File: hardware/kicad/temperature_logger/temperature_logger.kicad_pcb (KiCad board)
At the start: 2 copper layers, 40 x 64 mm, 45 parts, among them J1 SWD, J2 Power, J3 USB_B_Micro, J4 UART, Q1 Q_PMOS_DGS, SW1 UserBtn, U1 TMP112, U2 MX25R1635FM1IL0, U3 STM32L053C8Tx, U4 AMS1117-3.3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

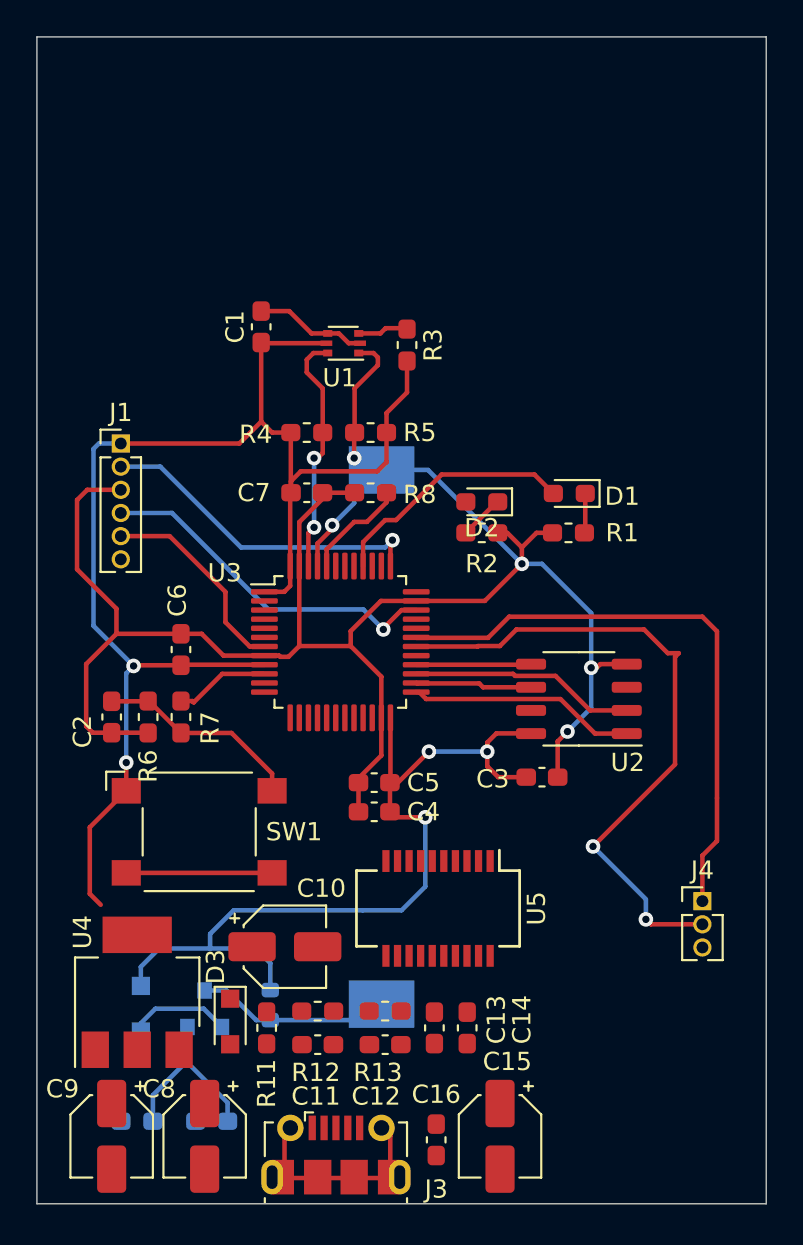
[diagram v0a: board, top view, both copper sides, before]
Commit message: Main rounting done for pass 2
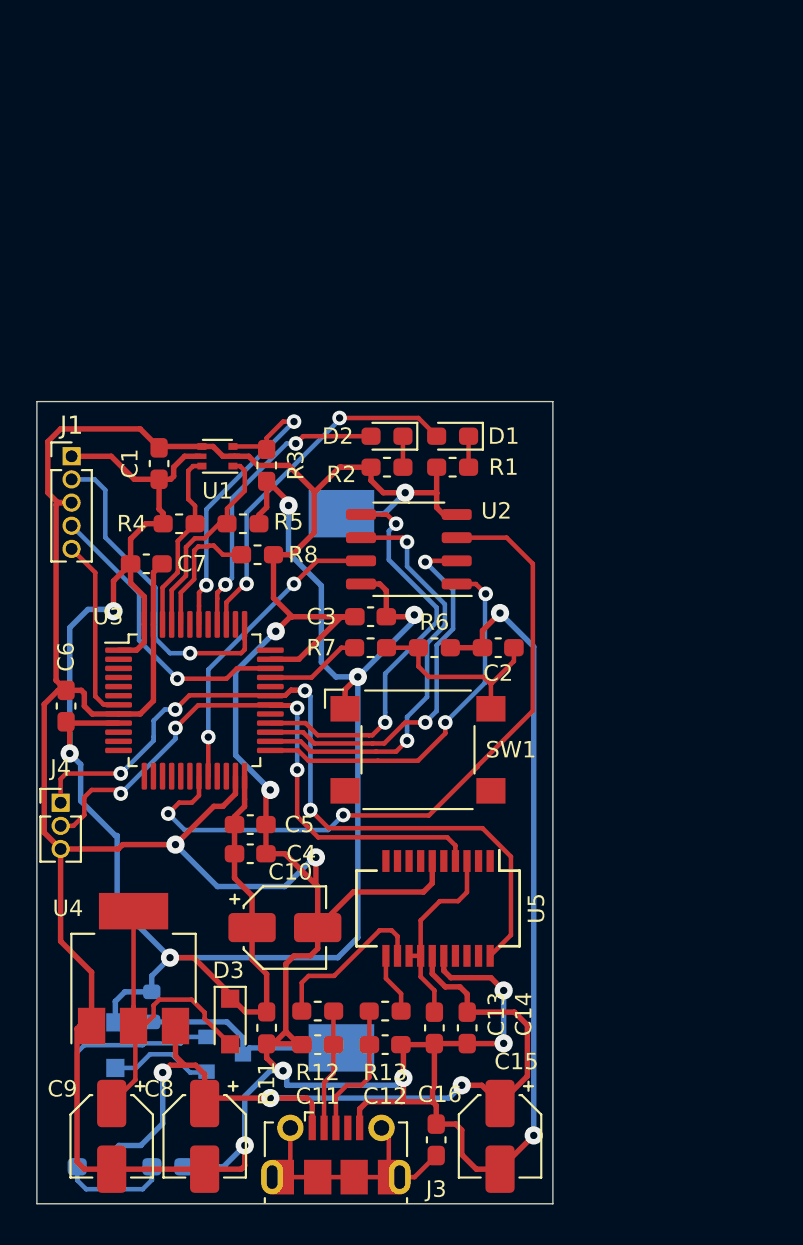
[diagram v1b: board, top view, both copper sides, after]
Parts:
- J1: footprint Connector_PinHeader_1.27mm:PinHeader_1x06_P1.27mm_Vertical -> Connector_PinHeader_1.27mm:PinHeader_1x05_P1.27mm_Vertical
- moved J4 35.6 mm to (131.3, 88.0)
- moved C2 21.5 mm to (155.3, 79.5), turned to 0 degrees
- moved R6 16.2 mm to (151.8, 79.5), turned to 0 degrees
- moved C3 12.9 mm to (148.3, 77.8), turned to 180 degrees
- moved SW1 12.8 mm to (150.9, 85.1)
- moved U2 12.4 mm to (150.4, 74.1)
- moved R7 11.1 mm to (148.3, 79.5), turned to 0 degrees
- moved R3 10.1 mm to (142.6, 69.5)
- moved C7 9.63 mm to (136.0, 74.9)
- moved C1 9.36 mm to (136.7, 69.4)
- moved U1 9.28 mm to (139.9, 69.0)
- moved U3 8.62 mm to (138.6, 82.4)
- moved R4 8.60 mm to (137.8, 72.7)
- moved R5 8.60 mm to (141.3, 72.7)
- moved R1 7.30 mm to (152.8, 69.6)
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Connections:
- U3 pad 10: /USER_BTN -> (no net)
- U3 pad 15: /USER_LED1 -> (no net)
- U3 pad 18: /TMP_ALERT -> (no net)
- U3 pad 33: (no net) -> /USER_BTN
- U3 pad 39: (no net) -> /USER_LED2
- U3 pad 40: /USER_LED2 -> /USER_LED1
- U3 pad 42: (no net) -> /TMP_ALERT
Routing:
- net GND: track 104.1 -> 268.6 mm, vias 3 -> 12
- net VBUS: track 0.00 -> 47.5 mm, vias 0 -> 3
- net /FLASH_WPN: track 0.00 -> 39.1 mm, vias 0 -> 2
- net Net-(C9-Pad1): track 0.00 -> 18.9 mm
- net /FLASH_SCLK: track 6.40 -> 23.3 mm, vias 0 -> 2
- net /FLASH_RSTN: track 0.00 -> 16.7 mm, vias 0 -> 2
- net /USER_LED1: track 0.00 -> 16.3 mm, vias 0 -> 2
- net /FLASH_SI: track 6.31 -> 22.3 mm, vias 0 -> 2
- net /TMP_ALERT: track 2.79 -> 17.7 mm, vias 0 -> 2
- net /USART1_RX: track 32.5 -> 44.1 mm, vias 0 -> 4
- net Net-(C13-Pad1): track 0.00 -> 10.9 mm
- net Net-(Q1-Pad2): track 10.2 -> 19.7 mm
- net Net-(R12-Pad2): track 0.00 -> 9.21 mm
- net /FLASH_SO: track 12.4 -> 21.0 mm, vias 0 -> 2
- net /FLASH_CSN: track 12.5 -> 20.8 mm, vias 0 -> 2
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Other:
- board size 40 x 64 mm -> 28.3 x 44 mm
- net class Power added: clearance 0.2, trace_width 0.3, via_dia 1, via_drill 0.4
- board text added: "TempPal v1.0"

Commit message: Hardware routing completed (verification required)
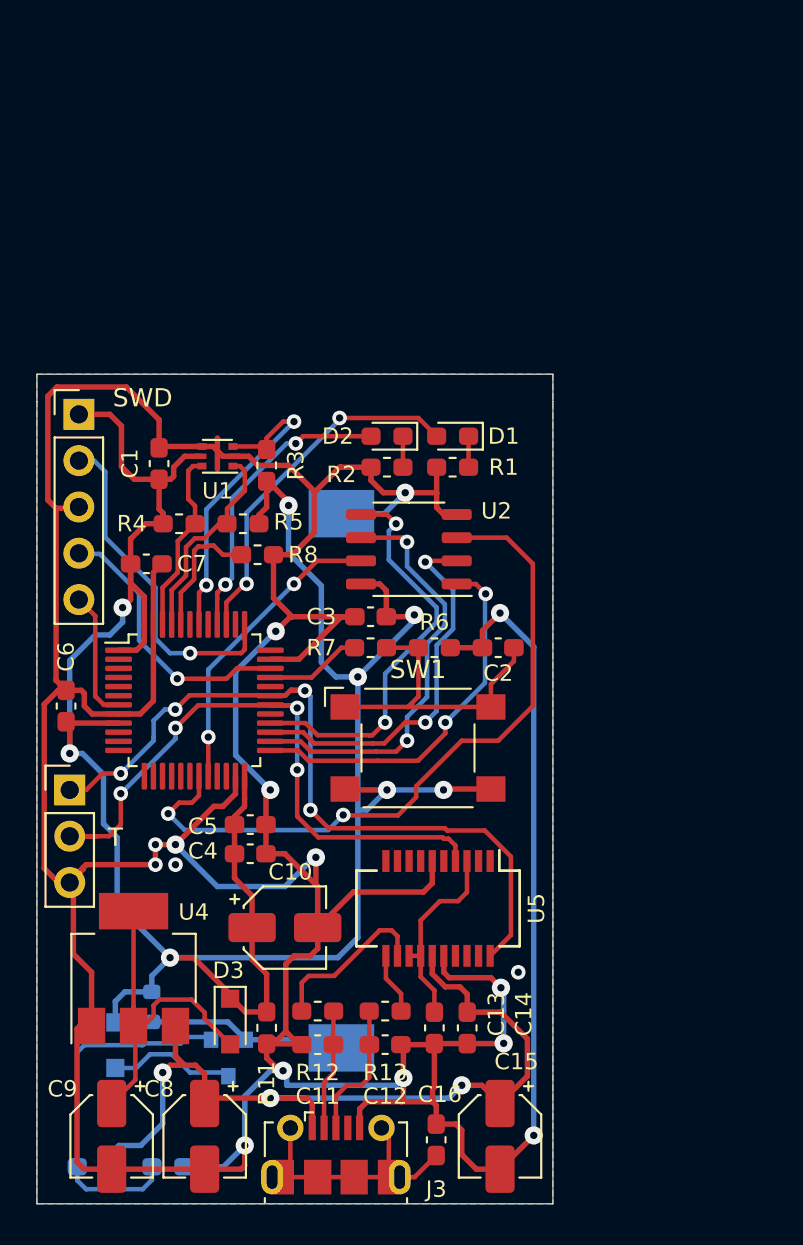
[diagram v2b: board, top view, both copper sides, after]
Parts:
- J1: footprint Connector_PinHeader_1.27mm:PinHeader_1x05_P1.27mm_Vertical -> Connector_PinHeader_2.54mm:PinHeader_1x05_P2.54mm_Vertical
- J4: footprint Connector_PinHeader_1.27mm:PinHeader_1x03_P1.27mm_Vertical -> Connector_PinHeader_2.54mm:PinHeader_1x03_P2.54mm_Vertical
- Q1: value Q_PMOS_DGS -> Q_PMOS_GSD
- SW1: value UserBtn -> SW_MEC_5E
- moved J1 2.33 mm to (132.3, 66.7)
- moved J4 0.86 mm to (131.8, 87.3)
- moved Q1 0.28 mm to (140.5, 102.0), turned to 270 degrees
- moved SW1 0.10 mm to (150.9, 85.0)
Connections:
- Q1 pad 1: Net-(D4-Pad2) -> Net-(Q1-Pad1)
- Q1 pad 2: Net-(Q1-Pad2) -> +BATT
- Q1 pad 3: +BATT -> Net-(D4-Pad2)
- R10 pad 1: Net-(Q1-Pad2) -> Net-(Q1-Pad1)
- R9 pad 2: Net-(Q1-Pad2) -> Net-(Q1-Pad1)
- SW1 pad 1: VDC -> Net-(C2-Pad2)
- SW1 pad 3: (no net) -> VDC
- SW1 pad 4: (no net) -> VDC
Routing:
- net Net-(Q1-Pad1): track 0.00 -> 20.0 mm
- net Net-(Q1-Pad2): track 19.7 -> 0.00 mm
- net VDC: track 130.5 -> 140.3 mm, vias 6 -> 8
- net GND: track 268.6 -> 276.8 mm, vias 12 -> 16
- net Net-(C2-Pad2): track 11.0 -> 17.1 mm
- net /NRESET: track 10.1 -> 7.15 mm
- net /USART1_TX: track 34.5 -> 35.9 mm
- net Net-(D4-Pad2): track 5.75 -> 7.01 mm
- net /SWDIO: track 16.1 -> 15.1 mm
- net +BATT: track 11.8 -> 11.0 mm
- net /SWCLK: track 18.1 -> 18.7 mm
- added copper zone on B.Cu, net GND
- added copper zone on F.Cu, net GND
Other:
- board size 28.3 x 44 mm -> 28.3 x 45.5 mm
- board text added: "SWD"
- board text added: "T"

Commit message: Extracted footprints and schematics
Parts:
- C1, C11, C12, C13, C14, C16, C2, C3, C4, C5, C6, C7: footprint Capacitor_SMD:C_0603_1608Metric_Pad1.08x0.95mm_HandSolder -> Library:C_0603_1608Metric_Pad1.08x0.95mm_HandSolder
- C10, C15, C8, C9: footprint Capacitor_SMD:CP_Elec_4x5.7 -> Library:CP_Elec_4x5.7
- D1, D2: footprint LED_SMD:LED_0603_1608Metric_Pad1.05x0.95mm_HandSolder -> Library:LED_0603_1608Metric_Pad1.05x0.95mm_HandSolder
- D3, D4: footprint Diode_SMD:D_SOD-323_HandSoldering -> Library:D_SOD-323_HandSoldering
- J1: footprint Connector_PinHeader_2.54mm:PinHeader_1x05_P2.54mm_Vertical -> Library:PinHeader_1x05_P2.54mm_Vertical
- J2: footprint Battery:BatteryHolder_Keystone_1060_1x2032 -> Library:BatteryHolder_Keystone_1060_1x2032
- J3: footprint Connector_USB:USB_Micro-B_Molex-105017-0001 -> Library:USB_Micro-B_Molex-105017-0001
- J4: footprint Connector_PinHeader_2.54mm:PinHeader_1x03_P2.54mm_Vertical -> Library:PinHeader_1x03_P2.54mm_Vertical
- JP1: footprint Resistor_SMD:R_0603_1608Metric -> Library:R_0603_1608Metric
- Q1: footprint Package_TO_SOT_SMD:SOT-23 -> Library:SOT-23
- R1, R10, R11, R12, R13, R2, R3, R4, R5, R6, R7, R8, R9: footprint Resistor_SMD:R_0603_1608Metric_Pad1.05x0.95mm_HandSolder -> Library:R_0603_1608Metric_Pad1.05x0.95mm_HandSolder
- SW1: footprint Button_Switch_SMD:SW_SPST_Omron_B3FS-101xP -> Library:SW_SPST_Omron_B3FS-101xP
- U1: footprint Package_TO_SOT_SMD:SOT-666 -> Library:SOT-666
- U2: footprint Package_SO:SOP-8_3.9x4.9mm_P1.27mm -> Library:SOP-8_3.9x4.9mm_P1.27mm
- U3: footprint Package_QFP:LQFP-48_7x7mm_P0.5mm -> Library:LQFP-48_7x7mm_P0.5mm
- U4: footprint Package_TO_SOT_SMD:SOT-223-3_TabPin2 -> Library:SOT-223-3_TabPin2
- U5: footprint Package_SO:SSOP-20_3.9x8.7mm_P0.635mm -> Library:SSOP-20_3.9x8.7mm_P0.635mm
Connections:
- J3 pad 4: (no net) -> unconnected-(J3-Pad4)
- U3 pad 10: (no net) -> unconnected-(U3-Pad10)
- U3 pad 11: (no net) -> unconnected-(U3-Pad11)
- U3 pad 12: (no net) -> unconnected-(U3-Pad12)
- U3 pad 13: (no net) -> unconnected-(U3-Pad13)
- U3 pad 14: (no net) -> unconnected-(U3-Pad14)
- U3 pad 15: (no net) -> unconnected-(U3-Pad15)
- U3 pad 16: (no net) -> unconnected-(U3-Pad16)
- U3 pad 17: (no net) -> unconnected-(U3-Pad17)
- U3 pad 18: (no net) -> unconnected-(U3-Pad18)
- U3 pad 2: (no net) -> unconnected-(U3-Pad2)
- U3 pad 21: (no net) -> unconnected-(U3-Pad21)
- U3 pad 22: (no net) -> unconnected-(U3-Pad22)
- U3 pad 29: (no net) -> unconnected-(U3-Pad29)
- U3 pad 3: (no net) -> unconnected-(U3-Pad3)
- U3 pad 32: (no net) -> unconnected-(U3-Pad32)
- U3 pad 36: (no net) -> unconnected-(U3-Pad36)
- U3 pad 38: (no net) -> unconnected-(U3-Pad38)
- U3 pad 4: (no net) -> unconnected-(U3-Pad4)
- U3 pad 41: (no net) -> unconnected-(U3-Pad41)
- U3 pad 43: (no net) -> unconnected-(U3-Pad43)
- U3 pad 5: (no net) -> unconnected-(U3-Pad5)
- U3 pad 6: (no net) -> unconnected-(U3-Pad6)
- U5 pad 1: (no net) -> unconnected-(U5-Pad1)
- U5 pad 10: (no net) -> unconnected-(U5-Pad10)
- U5 pad 17: (no net) -> unconnected-(U5-Pad17)
- U5 pad 18: (no net) -> unconnected-(U5-Pad18)
- U5 pad 19: (no net) -> unconnected-(U5-Pad19)
- U5 pad 2: (no net) -> unconnected-(U5-Pad2)
- U5 pad 5: (no net) -> unconnected-(U5-Pad5)
- U5 pad 7: (no net) -> unconnected-(U5-Pad7)
- U5 pad 8: (no net) -> unconnected-(U5-Pad8)
- U5 pad 9: (no net) -> unconnected-(U5-Pad9)
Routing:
- net /USART1_RX: track 44.5 -> 43.8 mm
- net VDC: track 140.3 -> 139.8 mm, vias 8 -> 7
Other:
- net class Default removed
- net class Power removed
